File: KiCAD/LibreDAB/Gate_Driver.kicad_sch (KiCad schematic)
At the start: 4 parts, among them U1 UCC27211DDAR

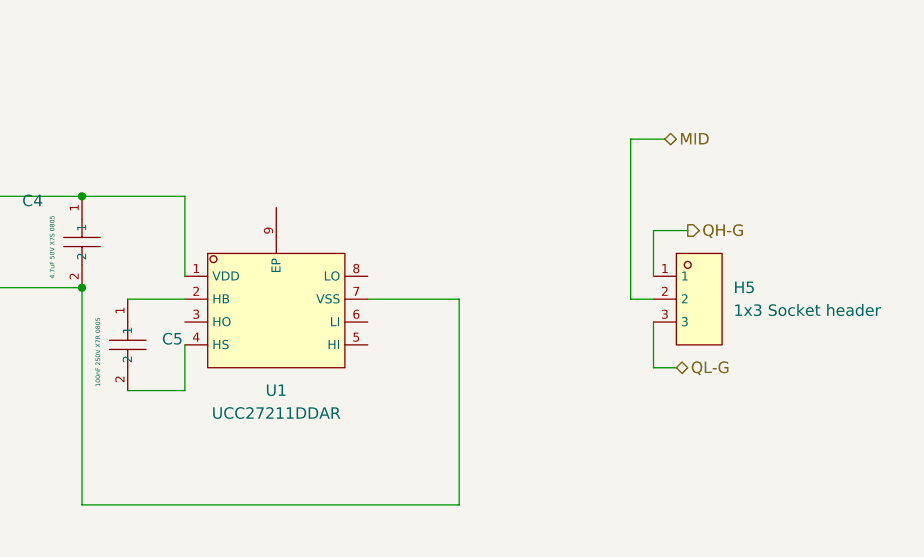
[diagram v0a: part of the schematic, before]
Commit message: Added more gate drive schematic info
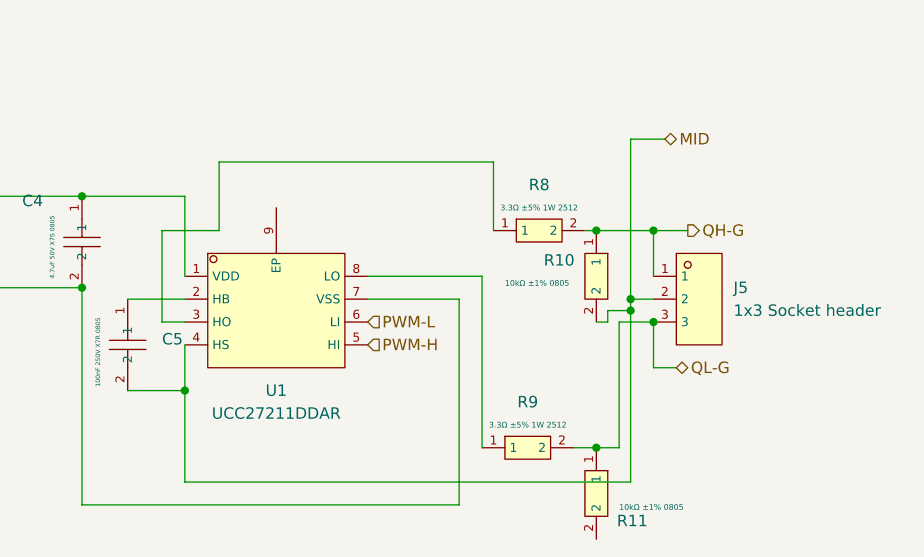
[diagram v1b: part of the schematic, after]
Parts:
- added R10, R11: 10kΩ ±1% 0805, lcsc_footprints:C2907219_R0805, symbol lcsc_imported:RES 10kΩ ±1% 125mW 0805
- added R8, R9: 3.3Ω ±5% 1W 2512, lcsc_footprints:C393074_RES-SMD_L6_4-W3_2-1, symbol lcsc_imported:1W_3.3Ω_200V_Thick_Film_Resistor_±400ppm/℃_±5%_2512_Chip_Resistor
- renumbered H5 to J5
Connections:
- net MID: now also C5.2, U1.4 (HS), R10.2
- net QH-G: now also R10.1, R8.2
- net QL-G: now also R11.1, R9.2
- net at U1.3 (HO): now also R8.1
- net PWM-H: now reaches U1.5 (HI)
- net PWM-L: now reaches U1.6 (LI)
- net at U1.8 (LO): now also R9.1

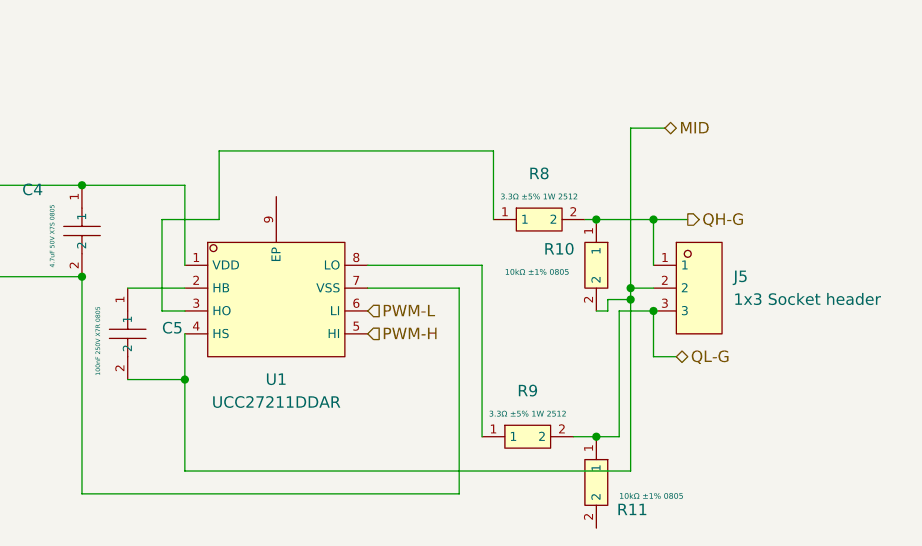
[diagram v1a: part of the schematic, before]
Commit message: Gate Drive schematic and footprints added
This is the last commit before trying the combined gate drive and sensing on the power board.
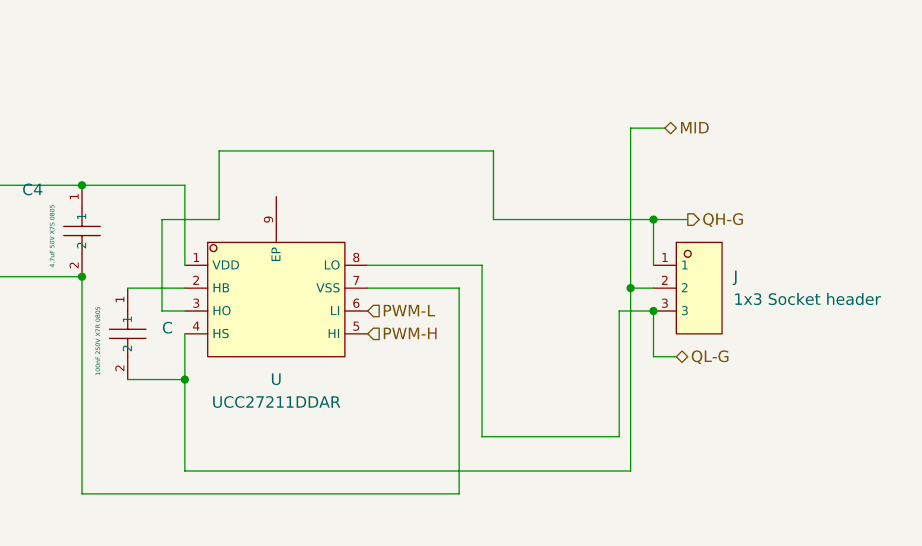
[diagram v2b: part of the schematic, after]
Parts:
- removed R10, R11: 10kΩ ±1% 0805, lcsc_footprints:C2907219_R0805, symbol lcsc_imported:RES 10kΩ ±1% 125mW 0805
- removed R8, R9: 3.3Ω ±5% 1W 2512, lcsc_footprints:C393074_RES-SMD_L6_4-W3_2-1, symbol lcsc_imported:1W_3.3Ω_200V_Thick_Film_Resistor_±400ppm/℃_±5%_2512_Chip_Resistor
- renumbered C5 to C, J5 to J, U1 to U
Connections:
- net QH-G: now also U.3 (HO)
- net QL-G: now also U.8 (LO)

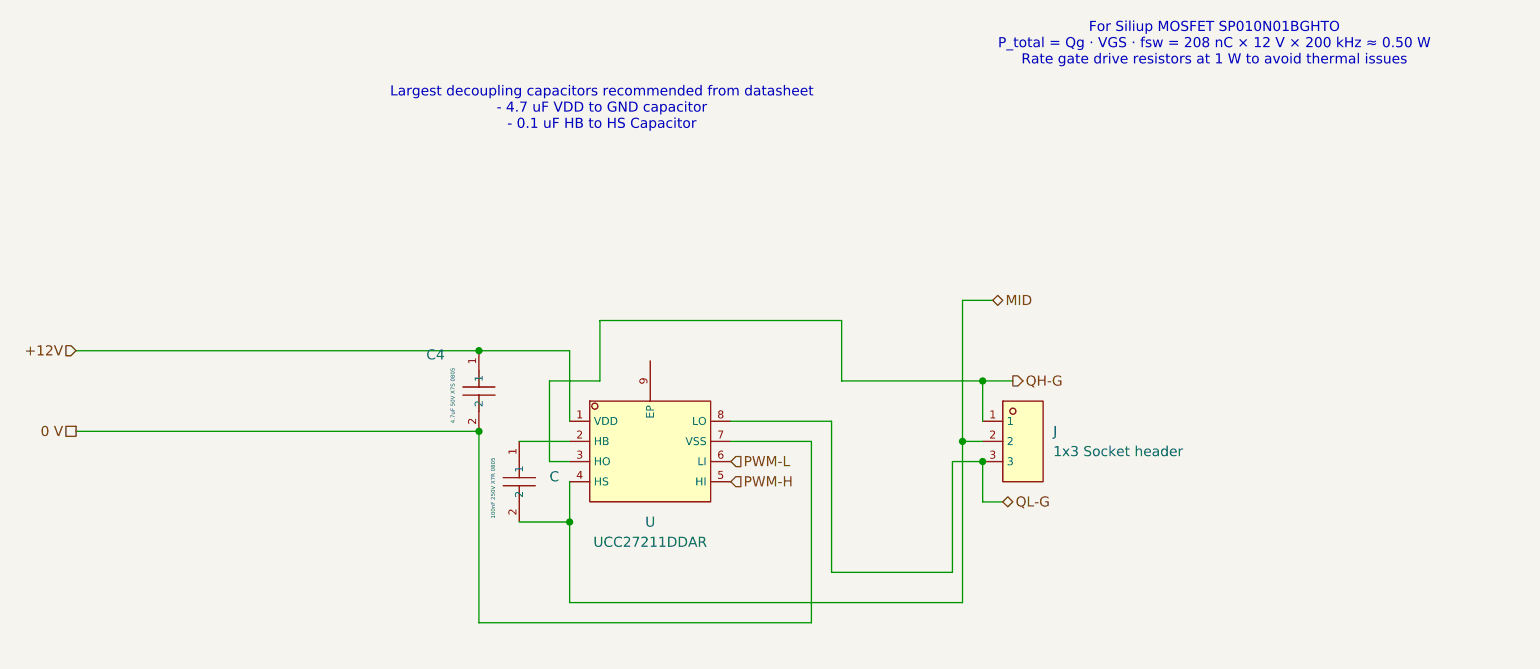
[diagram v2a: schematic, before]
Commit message: Edits to gate drive circuitry
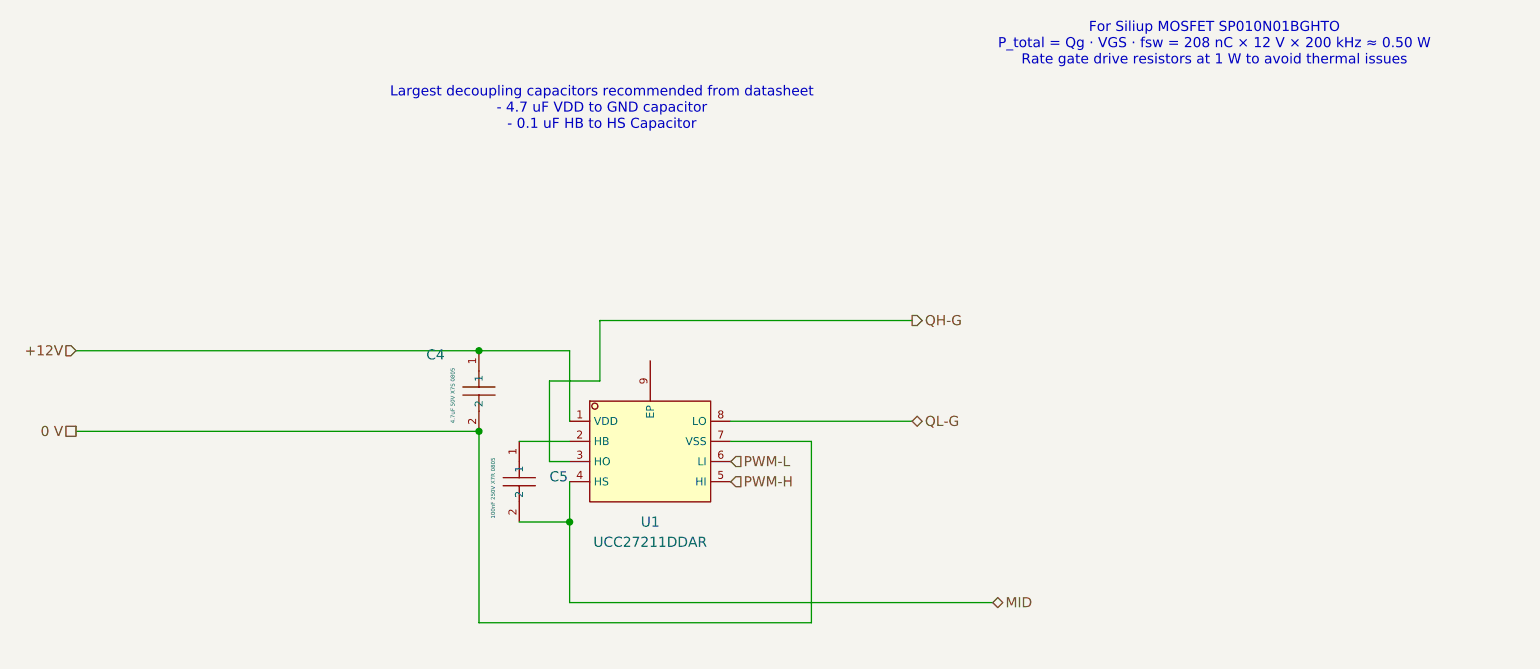
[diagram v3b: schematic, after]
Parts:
- removed J: 1x3 Socket header, lcsc_footprints:C46635839_HDR-SMD_3P-P2_54-V-F-LS4_7-6779753103411-RC, symbol lcsc_imported:HX_PM2_54-1X3P_TP_H8_5-YQ
- renumbered C to C5, U to U1

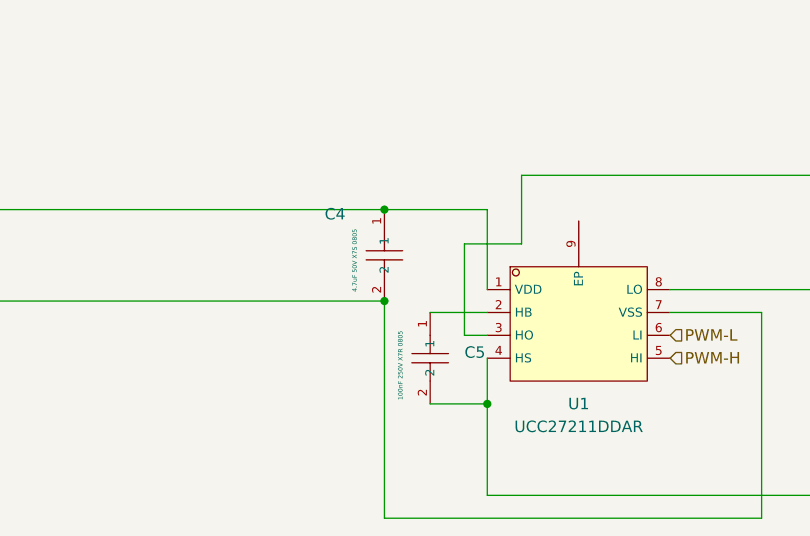
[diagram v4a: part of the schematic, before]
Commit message: Annotation numbers reset
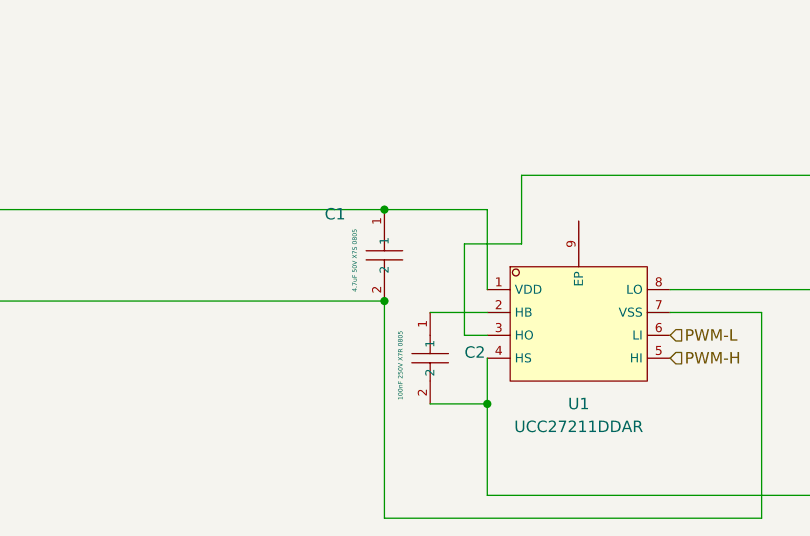
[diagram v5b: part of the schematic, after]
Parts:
- renumbered C4 to C1, C5 to C2
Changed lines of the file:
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@@
 		(on_board yes)
 		(dnp no)
-		(property "Reference" "C5"
+		(property "Reference" "C2"
 			(at 129.54 85.7249 90)
 			(effects
@@
 			(project ""
 				(path "/daf77073-b189-4351-8636-4e7a5198e1b7/f3c2518b-d41d-4c2c-ab2c-6739c5137e70/b5311c66-b122-4c07-875a-24692e20fcb9"
-					(reference "C5")
+					(reference "C2")
 					(unit 1)
 				)
 				(path "/daf77073-b189-4351-8636-4e7a5198e1b7/f3c2518b-d41d-4c2c-ab2c-6739c5137e70/f8c4e1d5-c720-4c36-bf5f-b4f0ce234f2f"
-					(reference "C6")
+					(reference "C12")
 					(unit 1)
 				)
@@
 		(on_board yes)
 		(dnp no)
-		(property "Reference" "C4"
+		(property "Reference" "C1"
 			(at 116.332 70.358 90)
 			(effects
@@
 			(project "LibreDAB"
 				(path "/daf77073-b189-4351-8636-4e7a5198e1b7/f3c2518b-d41d-4c2c-ab2c-6739c5137e70/b5311c66-b122-4c07-875a-24692e20fcb9"
-					(reference "C4")
+					(reference "C1")
 					(unit 1)
 				)
 				(path "/daf77073-b189-4351-8636-4e7a5198e1b7/f3c2518b-d41d-4c2c-ab2c-6739c5137e70/f8c4e1d5-c720-4c36-bf5f-b4f0ce234f2f"
-					(reference "C3")
+					(reference "C11")
 					(unit 1)
 				)
@@
 				)
 				(path "/daf77073-b189-4351-8636-4e7a5198e1b7/f3c2518b-d41d-4c2c-ab2c-6739c5137e70/f8c4e1d5-c720-4c36-bf5f-b4f0ce234f2f"
-					(reference "U2")
-					(unit 1)
-				)
+					(reference "U5")
+					(unit 1)
+				)

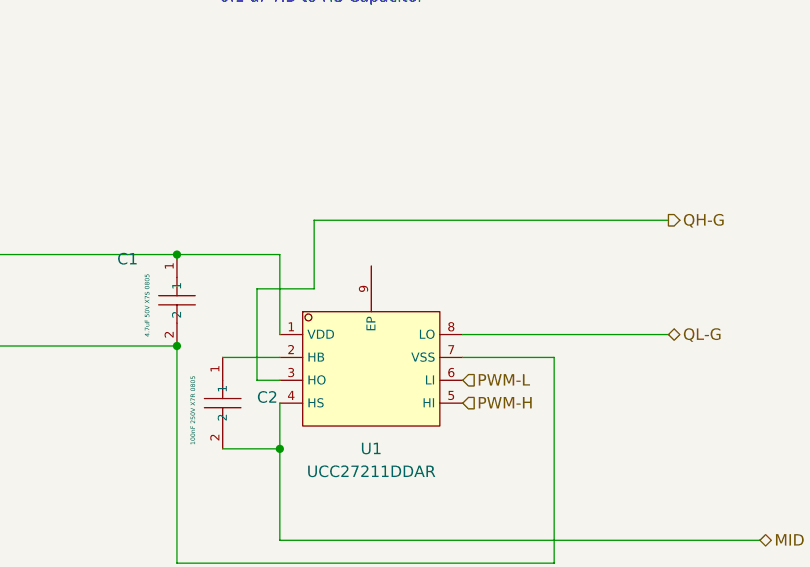
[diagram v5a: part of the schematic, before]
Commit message: PCB component placement on 92 x 92 mm board
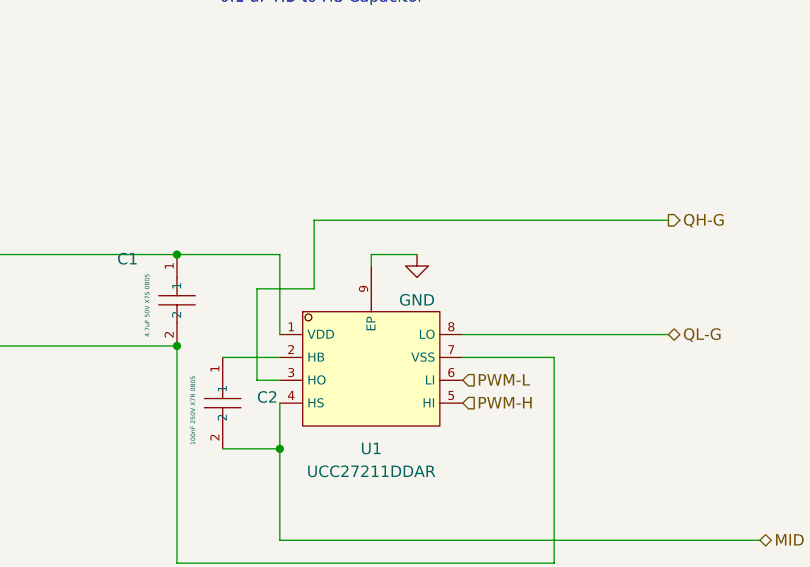
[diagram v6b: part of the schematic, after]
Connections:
- net GND: now reaches U1.9 (EP)
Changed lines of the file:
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@@
+	(wire
+		(pts
+			(xy 147.32 69.85) (xy 142.24 69.85)
+		)
+		(stroke
+			(width 0)
+			(type default)
+		)
+	)
 	(wire
 		(pts
 			(xy 132.08 83.82) (xy 129.54 83.82)
+		)
+		(stroke
+			(width 0)
+			(type default)
+		)
+	)
+	(wire
+		(pts
+			(xy 142.24 69.85) (xy 142.24 71.12)
 		)
 		(stroke
@@
 			)
 		)
+	)
+	(symbol
+		(lib_id "power:GND")
+		(at 147.32 69.85 0)
+		(unit 1)
+		(exclude_from_sim no)
+		(in_bom yes)
+		(on_board yes)
+		(dnp no)
+		(fields_autoplaced yes)
+		(property "Reference" "#PWR030"
+			(at 147.32 76.2 0)
+			(effects
+				(font
+					(size 1.27 1.27)
+				)
+				(hide yes)
+			)
+		)
+		(property "Value" "GND"
+			(at 147.32 74.93 0)
+			(effects
+				(font
+					(size 1.27 1.27)
+				)
+			)
+		)
+		(property "Footprint" ""
+			(at 147.32 69.85 0)
+			(effects
+				(font
+					(size 1.27 1.27)
+				)
+				(hide yes)
+			)
+		)
+		(property "Datasheet" ""
+			(at 147.32 69.85 0)
+			(effects
+				(font
+					(size 1.27 1.27)
+				)
+				(hide yes)
+			)
+		)
+		(property "Description" "Power symbol creates a global label with name \"GND\" , ground"
+			(at 147.32 69.85 0)
+			(effects
+				(font
+					(size 1.27 1.27)
+				)
+				(hide yes)
+			)
+		)
+		(pin "1"
+		)
+		(instances
+			(project ""
+				(path "/daf77073-b189-4351-8636-4e7a5198e1b7/f3c2518b-d41d-4c2c-ab2c-6739c5137e70/b5311c66-b122-4c07-875a-24692e20fcb9"
+					(reference "#PWR030")
+					(unit 1)
+				)
+				(path "/daf77073-b189-4351-8636-4e7a5198e1b7/f3c2518b-d41d-4c2c-ab2c-6739c5137e70/f8c4e1d5-c720-4c36-bf5f-b4f0ce234f2f"
+					(reference "#PWR031")
+					(unit 1)
+				)
+			)
+		)
